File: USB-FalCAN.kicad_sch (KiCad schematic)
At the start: 59 parts, among them J1 Conn_01x17_Pin, J10 CAN, J2 NC, J3 Conn_01x17_Pin, J4 USB2.0_16P, J5 Boot, J6 NC, J7 DE9_Receptacle, J8 RS-485/422-TX, J9 RS-422-RX, SW3 BTN, U1 STM32F042C6Tx, U2 SN65HVD230, U3 SP3485EN, U4 SP3485EN, U5 MIC5504-3.3YM5, Y1 8MHz, Y2 32768Hz

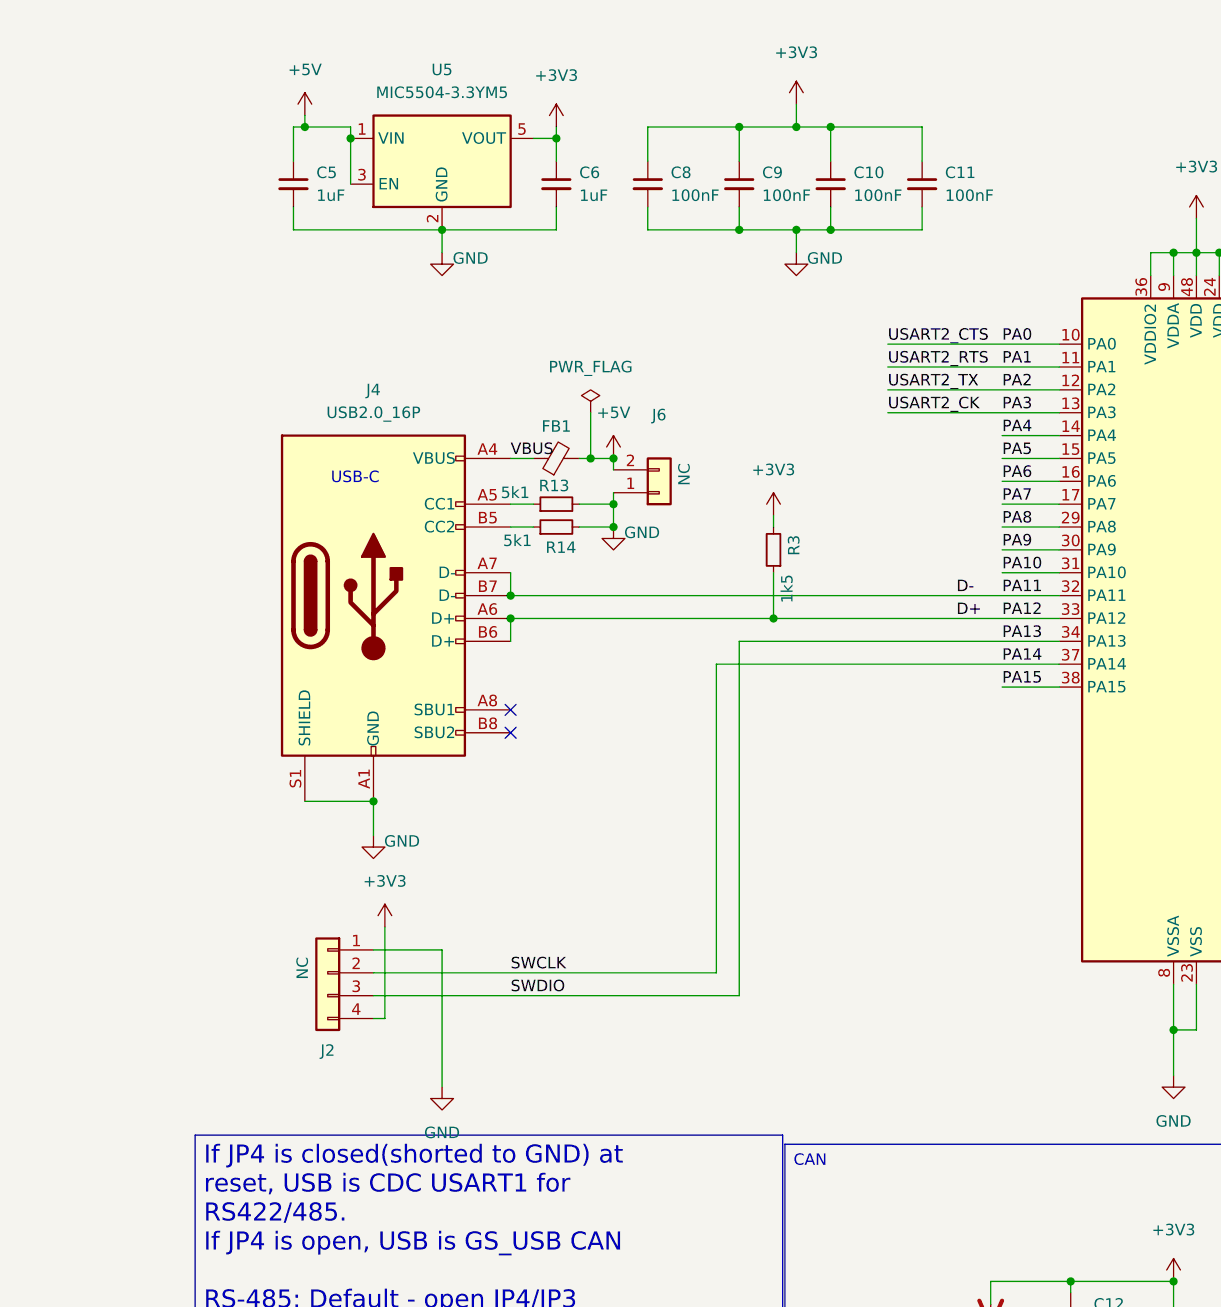
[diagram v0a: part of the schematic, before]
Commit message: feat: Change to male D-sub, fix "B3" silk
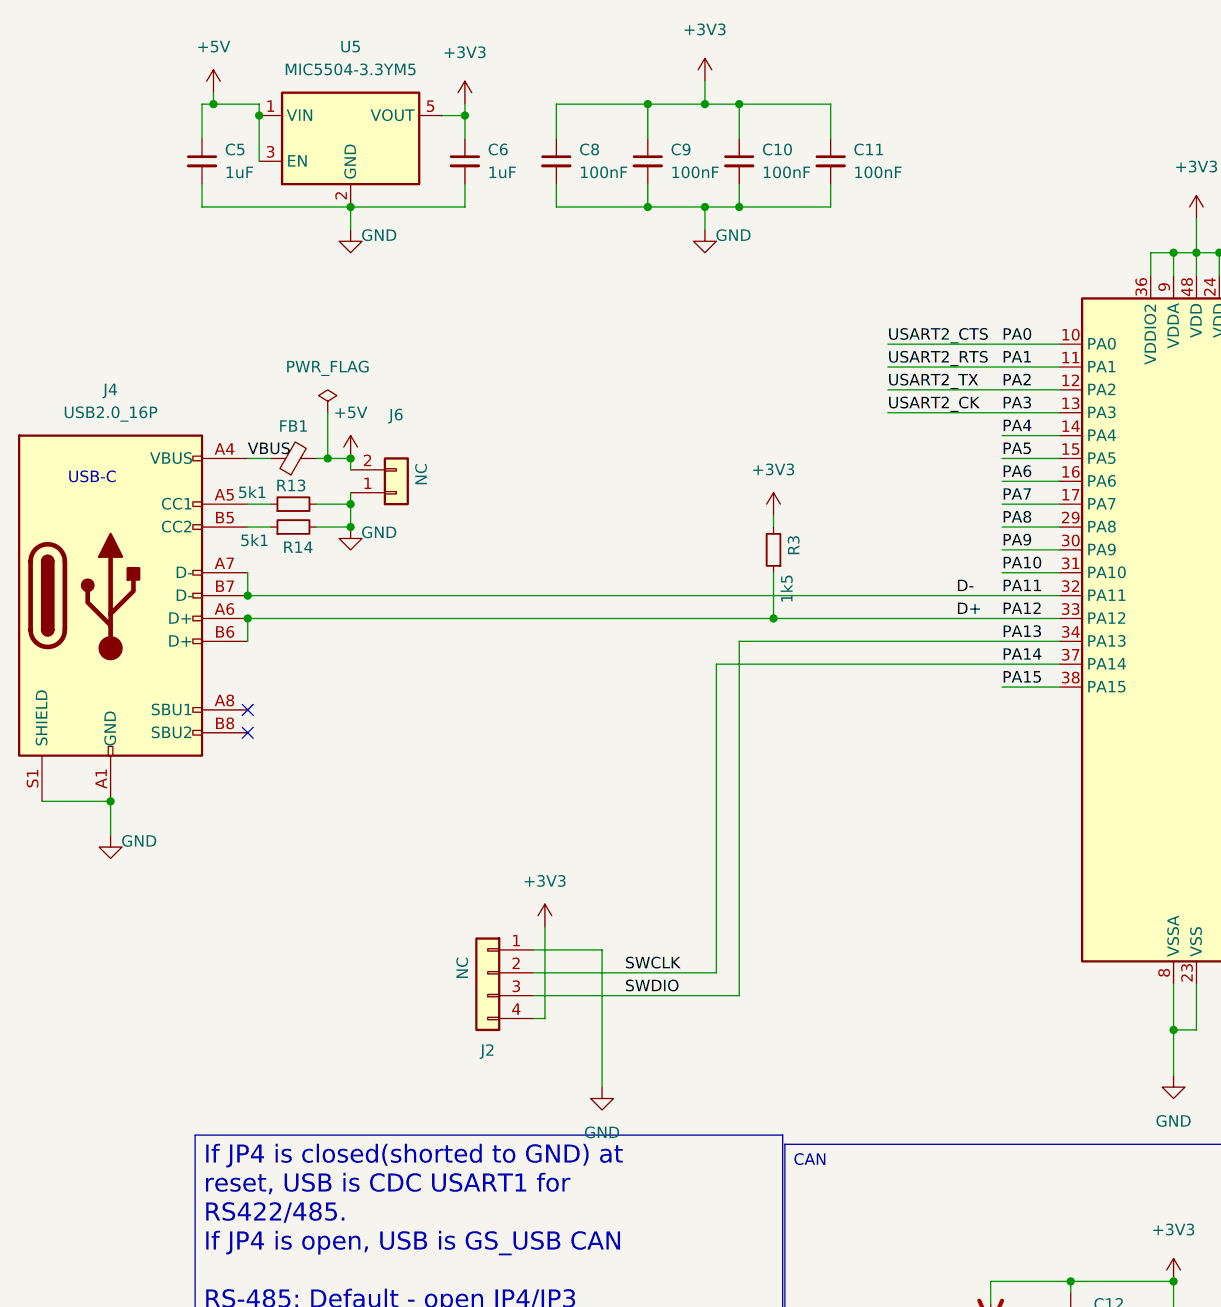
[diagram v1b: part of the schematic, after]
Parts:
- J7: footprint Connector_Dsub:DSUB-9_Female_Horizontal_P2.77x2.84mm_EdgePinOffset7.70mm_Housed_MountingHolesOffset9.12mm -> Connector_Dsub:DSUB-9_Pins_Horizontal_P2.77x2.84mm_EdgePinOffset7.70mm_Housed_MountingHolesOffset9.12mm
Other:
- moved on the sheet: C10, C11, C5, C6, C8, C9, FB1, J2, J4, J6, R13, R14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
